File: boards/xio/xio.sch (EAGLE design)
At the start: 295 parts, among them CN3 J00-0065NL, U2 LAN8742A-CZ, X2 USB-A, Y1 NX3225SA-12.000MHZ-STD-CSR-1, Y2 NX3225SA-12.000MHZ-STD-CSR-1, Y3 NX3225SA-25.000MHZ-STD-CSR-1

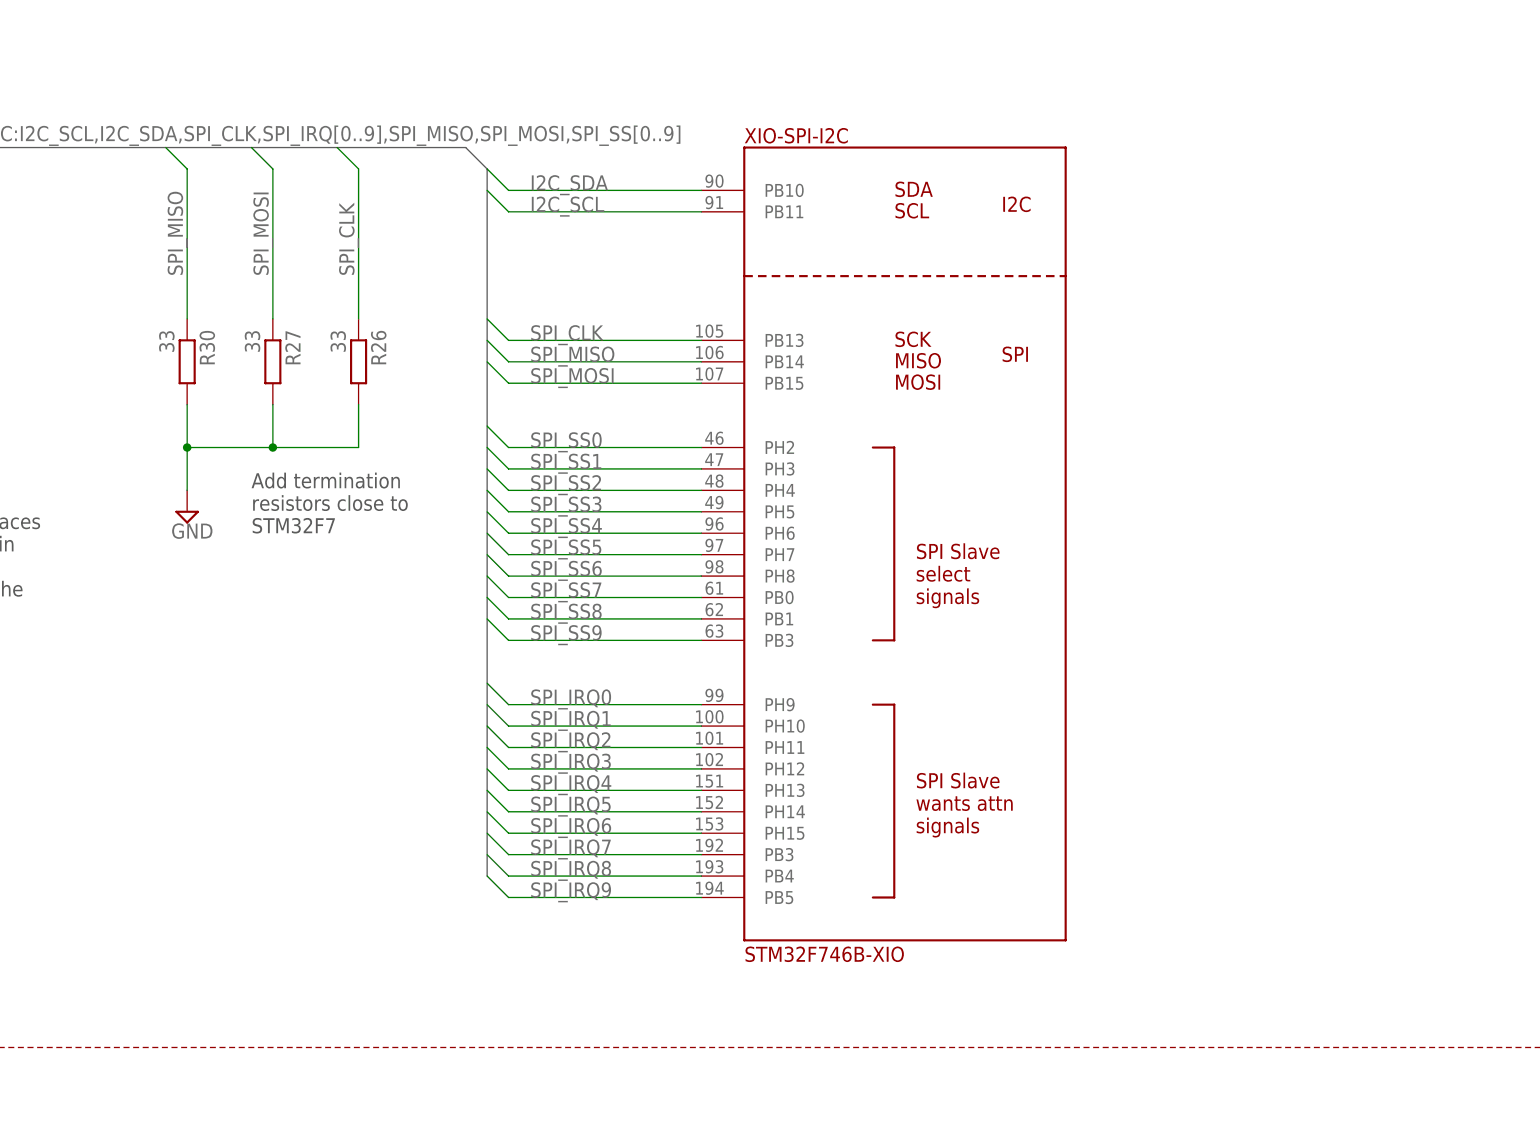
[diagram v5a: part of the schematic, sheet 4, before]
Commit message: Update schematics regarding comments and unroute board
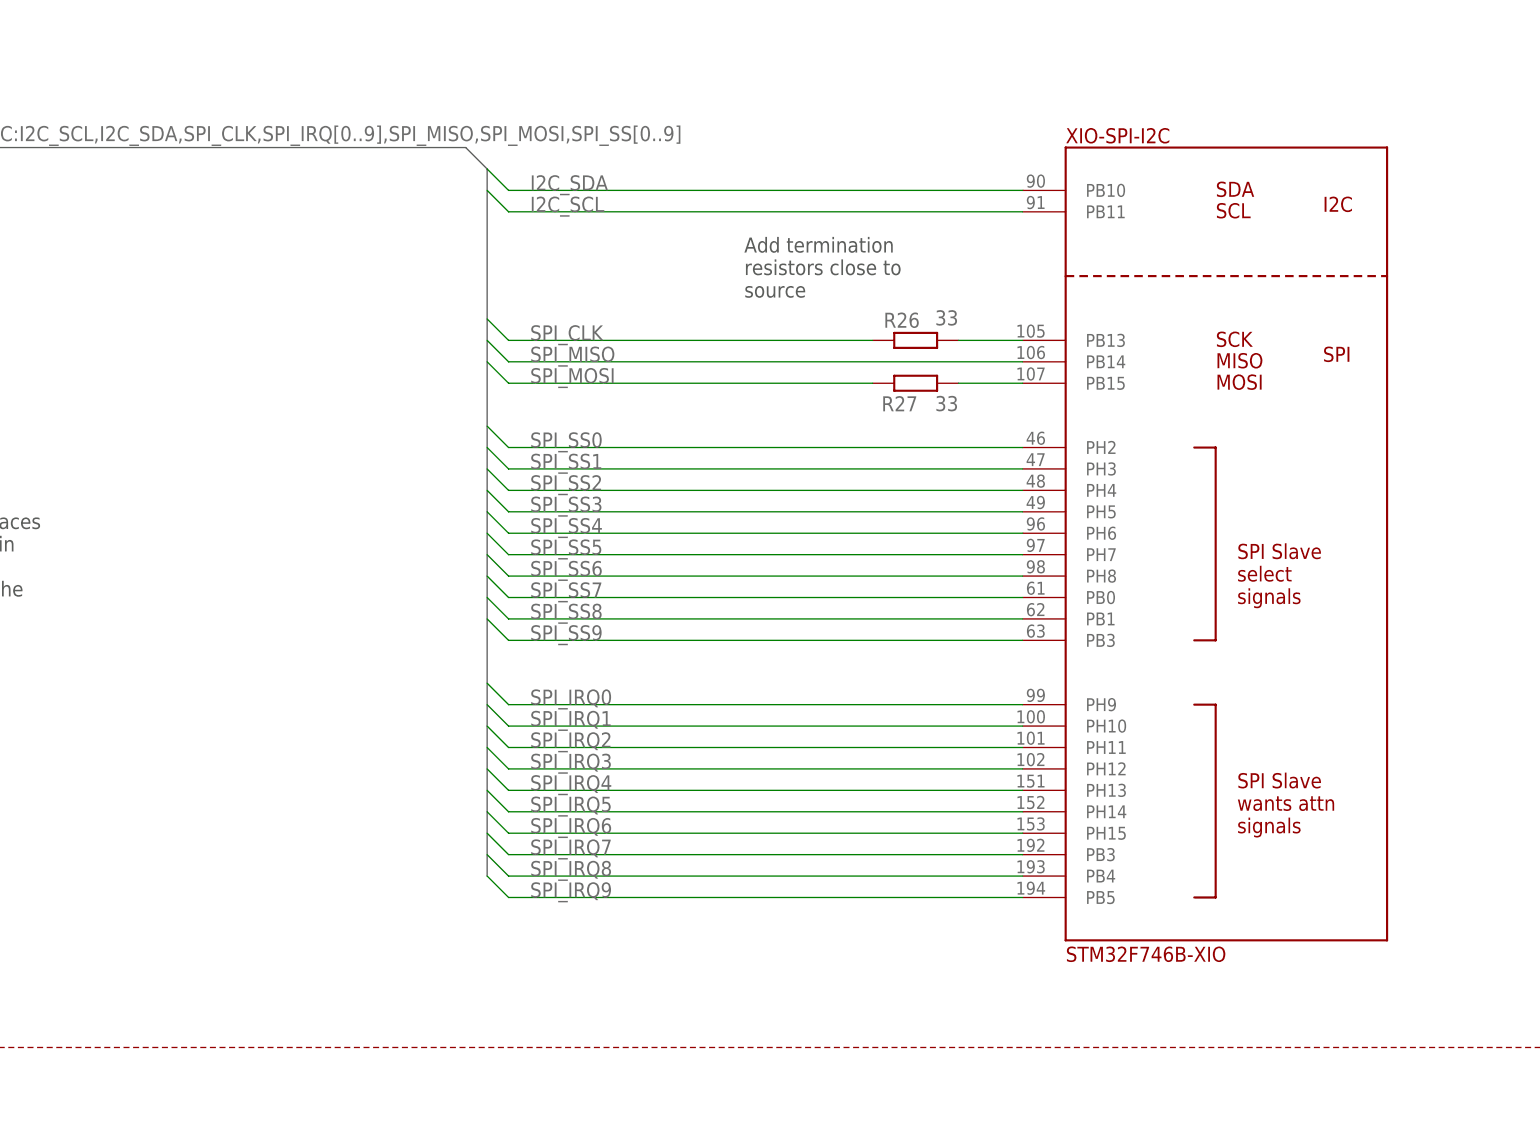
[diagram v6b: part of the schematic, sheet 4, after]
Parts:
- removed R30: 33, rcl:R-EU_R0402
- added R91: 33, rcl:R-EU_R0402
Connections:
- new net N$57: R26.2, XIO-SPI-I2C.PB13@105
- new net N$61: R27.2, XIO-SPI-I2C.PB15@107
- new net PIO_VDDA: C57.1, C58.1, PIO-POWER.VDDA@42, PIO-POWER.VREF+@41, R91.2
- net +3V3: now also R91.1; no longer C1.1, C13.1, C57.1, C58.1, PIO-POWER.VDDA@42, PIO-POWER.VREF+@41, XIO-POWER.VREF+@41
- net GND: no longer R26.2, R27.2, R30.2
- net SPI_CLK: no longer XIO-SPI-I2C.PB13@105
- net SPI_MISO: no longer R30.1
- net SPI_MOSI: no longer XIO-SPI-I2C.PB15@107
- net XIO_VDDA: now also C1.1, C13.1, XIO-POWER.VREF+@41
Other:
- note added: "- Added capacitor to +3v3 on SD_SLOT"
- note added: "- Added resistor in series to power on VDDA - Added pull-ups on /RESET and SWDIO - Added 0-ohm resistors on all power sources"
- note added: "Add termination resistors close to source"
- note added: "Filter on VDDA"
- note added: "Need ESD"
- note removed: "- Added capacitor to +3v3 on SD_SLOT - is 0.1uF sufficient ?"
- note removed: "- Added resistor in series to power on VDDA - is 33R ok ? - Added pull-ups on /RESET and SWDIO - Added 0-ohm resistors on all power sources"
- note removed: "- Need ESD ? What to do ?"
- note removed: "Add termination resistors close to STM32F7"
- note removed: "Anoop says "mended to add a filter on micro’s VDDA pin and connect the filter cap between VDDA and VSSA" - need to understand more"
- moved on the sheet: C1, C13, C57, C58, R21, R26, R27, XIO-SPI-I2C

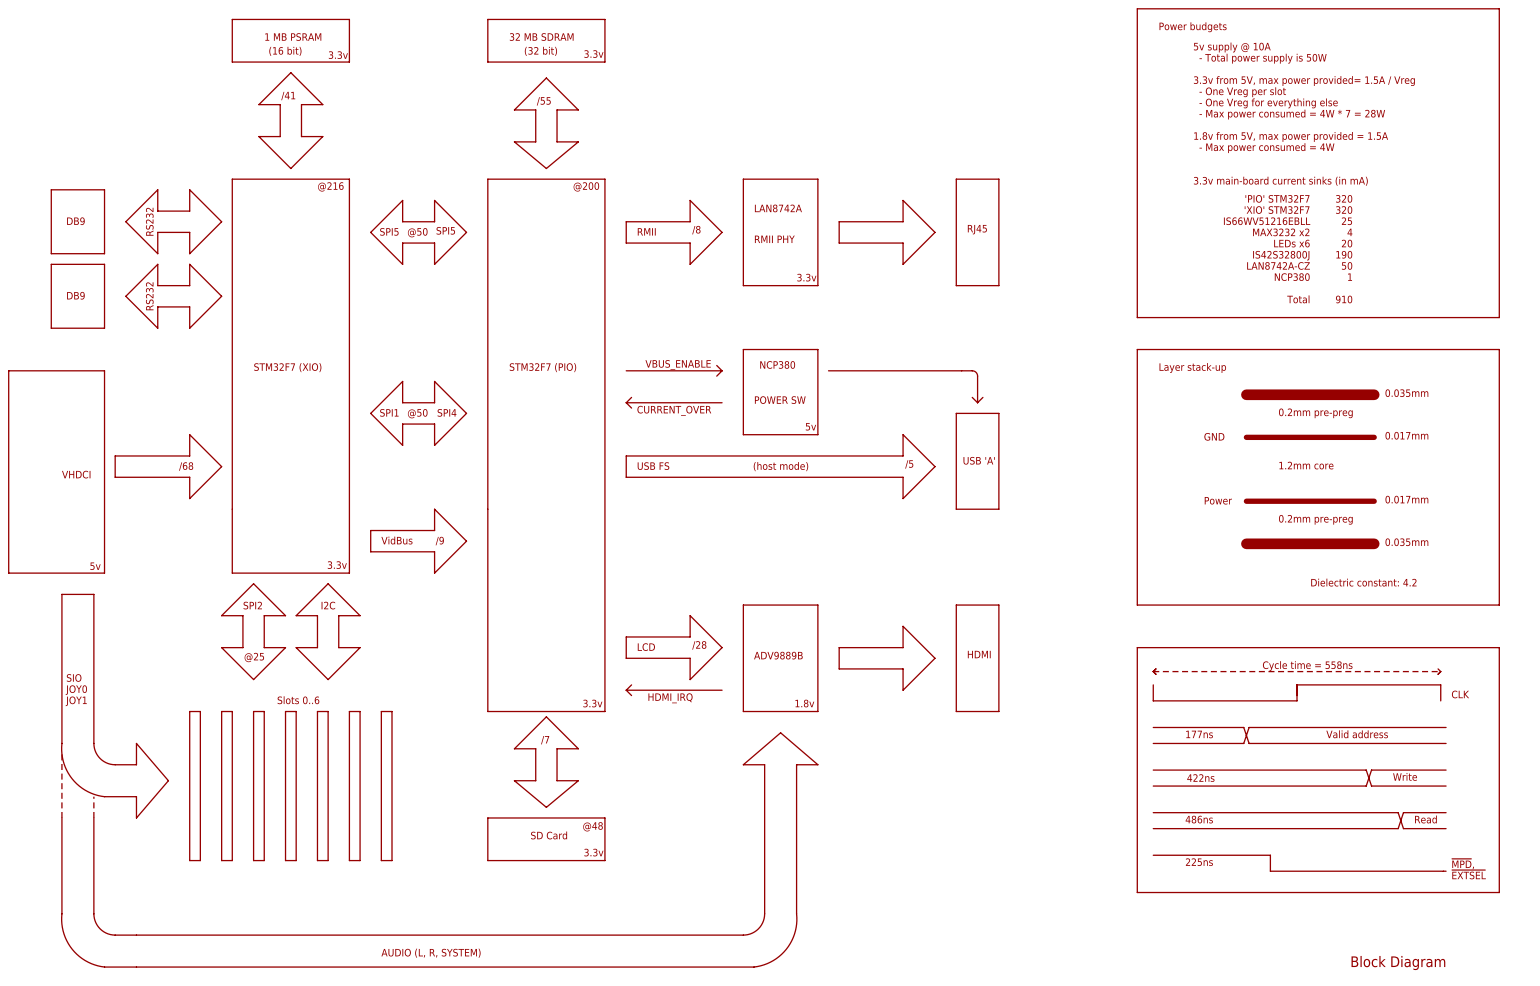
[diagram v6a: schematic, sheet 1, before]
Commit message: Start to patch in the H processor for XIO
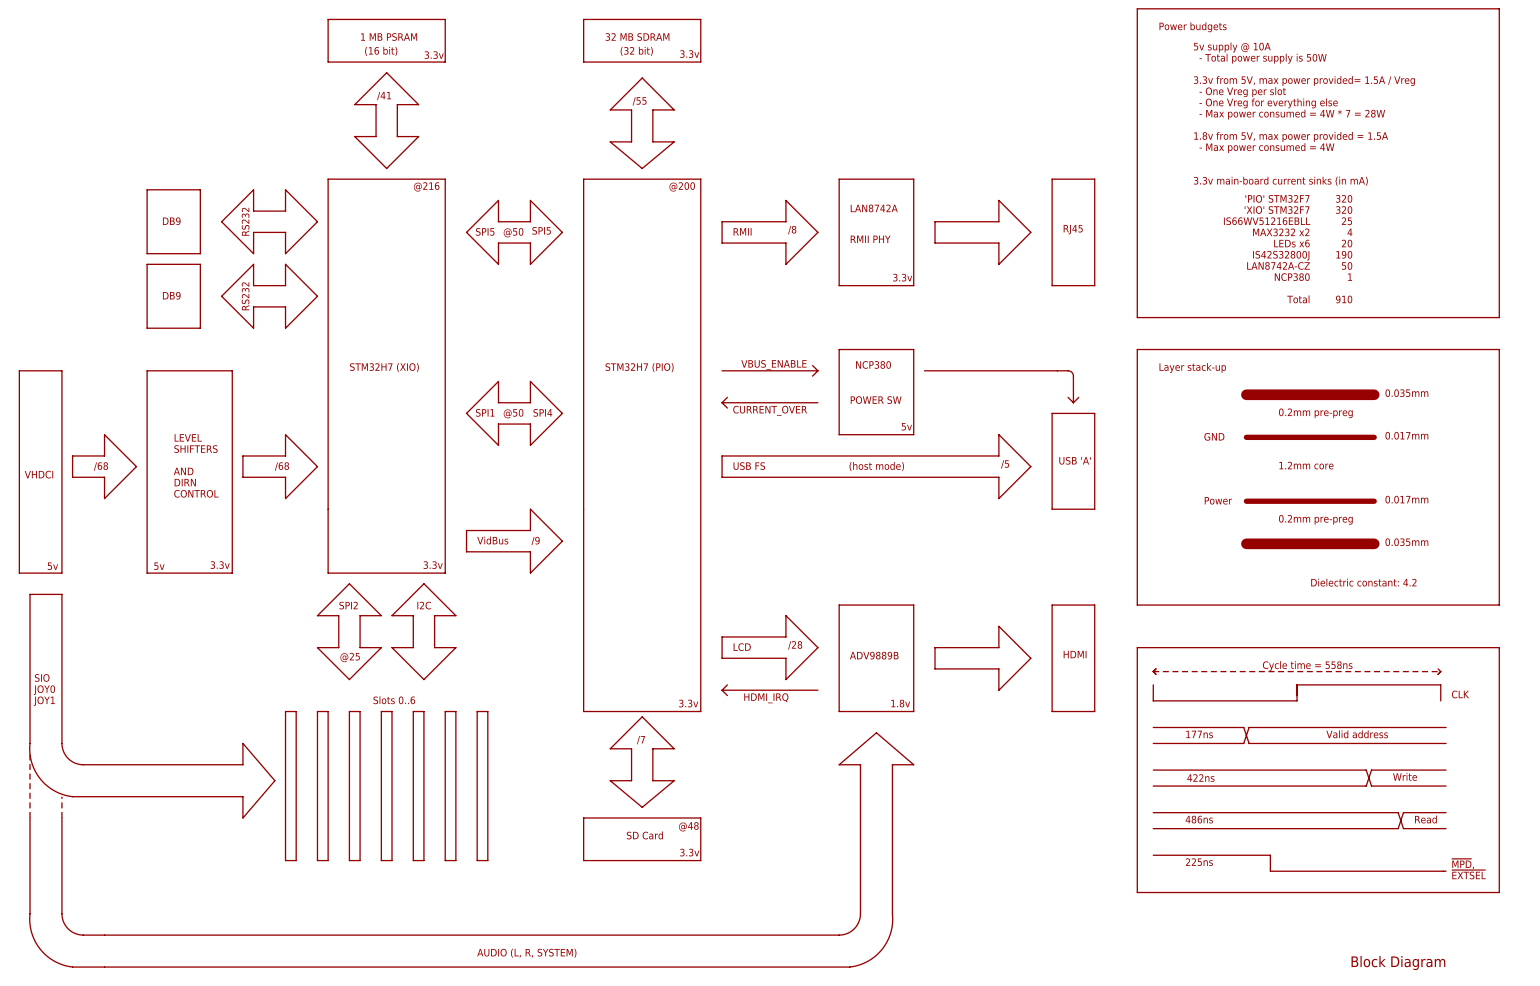
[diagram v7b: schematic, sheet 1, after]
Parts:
- removed R52: 33, rcl:R-EU_R0402
- XIO: value STM32F746B-XIO -> STM32H753B-XIO; device sjg-stm32:STM32F746B-XIO -> sjg-stm32:STM32H753B-XIO
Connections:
- removed net N$21: R52.2, XIO-VBUS.PJ15@177
- net !RESET!: now also XIO-PWR.!RST!@34; no longer XIO-POWER.!RST!@34
- net !VHDCI_EXSEL!: no longer XIO-VHDCI.PI8@7
- net !VHDCI_IRQ!: no longer XIO-VHDCI.PI9@11
- net !VHDCI_MPD!: no longer XIO-VHDCI.PI10@12
- net +3V3: now also XIO-PWR.VBAT@6, XIO-PWR.VDD@103, XIO-PWR.VDD@115, XIO-PWR.VDD@124, XIO-PWR.VDD@15, XIO-PWR.VDD@150, XIO-PWR.VDD@158, XIO-PWR.VDD@171, XIO-PWR.VDD@185, XIO-PWR.VDD@204, XIO-PWR.VDD@26, XIO-PWR.VDD@39, XIO-PWR.VDD@52, XIO-PWR.VDD@59, XIO-PWR.VDD@73, XIO-PWR.VDD@83, XIO-PWR.VDD@94, XIO-PWR.VDDUSB@137; no longer XIO-POWER.VBAT@6, XIO-POWER.VDD@103, XIO-POWER.VDD@115, XIO-POWER.VDD@124, XIO-POWER.VDD@15, XIO-POWER.VDD@150, XIO-POWER.VDD@158, XIO-POWER.VDD@171, XIO-POWER.VDD@185, XIO-POWER.VDD@204, XIO-POWER.VDD@26, XIO-POWER.VDD@39, XIO-POWER.VDD@52, XIO-POWER.VDD@59, XIO-POWER.VDD@73, XIO-POWER.VDD@83, XIO-POWER.VDD@94, XIO-POWER.VDDUSB@137
- net ARCH0: no longer XIO-CFG.PE2@1
- net ARCH1: no longer XIO-CFG.PE3@2
- net ARCH2: no longer XIO-CFG.PE4@3
- net ARCH3: no longer XIO-CFG.PE5@4
- net GND: now also XIO-PWR.VSS@114, XIO-PWR.VSS@125, XIO-PWR.VSS@136, XIO-PWR.VSS@14, XIO-PWR.VSS@149, XIO-PWR.VSS@170, XIO-PWR.VSS@184, XIO-PWR.VSS@202, XIO-PWR.VSS@25, XIO-PWR.VSS@51, XIO-PWR.VSS@60, XIO-PWR.VSS@72, XIO-PWR.VSS@82, XIO-PWR.VSS@93, XIO-PWR.VSSA@40; no longer XIO-POWER.VSS@114, XIO-POWER.VSS@125, XIO-POWER.VSS@136, XIO-POWER.VSS@14, XIO-POWER.VSS@149, XIO-POWER.VSS@170, XIO-POWER.VSS@184, XIO-POWER.VSS@202, XIO-POWER.VSS@25, XIO-POWER.VSS@51, XIO-POWER.VSS@60, XIO-POWER.VSS@72, XIO-POWER.VSS@82, XIO-POWER.VSS@93, XIO-POWER.VSSA@40
- net I2C_SCL: now also XIO-SPI_I2C.PB11@91; no longer XIO-SPI-I2C.PB11@91
- net I2C_SDA: now also XIO-SPI_I2C.PB10@90; no longer XIO-SPI-I2C.PB10@90
- net MEM0: no longer XIO-CFG.PF10@31
- net MEM1: no longer XIO-CFG.PF11@70
- net N$1: now also XIO-PWR.PH1@33; no longer XIO-POWER.PH1@33
- net N$11: now also XIO-PWR.BOOT0@197; no longer XIO-POWER.BOOT0@197
- net N$13: now also XIO-LED.PD5@169; no longer XIO-LED.PD2@166
- net N$14: now also XIO-LED.PD6@172; no longer XIO-LED.PD3@167
- net N$15: now also XIO-LED.PD7@173; no longer XIO-LED.PD6@172
- net N$18: no longer XIO-VHDCI.PJ0@65
- net N$2: now also XIO-PWR.PH0@32; no longer XIO-POWER.PH0@32
- net N$3: now also XIO-PWR.VCAP1@92; no longer XIO-POWER.VCAP1@92
- net N$34: now also XIO-USART.PA0@43; no longer XIO-UART.PA0@43
- net N$35: now also XIO-USART.PA3@50; no longer XIO-UART.PA3@50
- net N$39: now also XIO-USART.PA2@45; no longer XIO-UART.PA2@45
- net N$40: now also XIO-USART.PA1@44; no longer XIO-UART.PA1@44
- net N$47: now also XIO-USART.PG13@182; no longer XIO-UART.PG13@182
- net N$48: now also XIO-USART.PG9@178; no longer XIO-UART.PG9@178
- net N$49: now also XIO-USART.PG14@183; no longer XIO-UART.PG14@183
- net N$5: now also XIO-PWR.VCAP2@148; no longer XIO-POWER.VCAP2@148
- net N$50: now also XIO-USART.PG12@181; no longer XIO-UART.PG12@181
- net N$57: now also XIO-SPI_I2C.PB13@105; no longer XIO-SPI-I2C.PB13@105
- net N$61: now also XIO-SPI_I2C.PB15@107; no longer XIO-SPI-I2C.PB15@107
- net N$7: now also XIO-PWR.PDR_ON@203; no longer XIO-POWER.PDR_ON@203
- net PID0: no longer XIO-CFG.PG10@179
- net PID1: no longer XIO-CFG.PG11@180
- net PID2: no longer XIO-CFG.PG15@191
- net SPI_IRQ0: now also XIO-SPI_I2C.PH9@99; no longer XIO-SPI-I2C.PH9@99
- net SPI_IRQ1: now also XIO-SPI_I2C.PH10@100; no longer XIO-SPI-I2C.PH10@100
- net SPI_IRQ2: now also XIO-SPI_I2C.PH11@101; no longer XIO-SPI-I2C.PH11@101
- net SPI_IRQ3: now also XIO-SPI_I2C.PH12@102; no longer XIO-SPI-I2C.PH12@102
- net SPI_IRQ4: now also XIO-SPI_I2C.PH13@151; no longer XIO-SPI-I2C.PH13@151
- net SPI_IRQ5: now also XIO-SPI_I2C.PH14@152; no longer XIO-SPI-I2C.PH14@152
- net SPI_IRQ6: now also XIO-SPI_I2C.PH15@153; no longer XIO-SPI-I2C.PH15@153
- net SPI_IRQ7: now also XIO-SPI_I2C.PB5@194; no longer XIO-SPI-I2C.PB3@192
- net SPI_IRQ8: now also XIO-SPI_I2C.PG6@133; no longer XIO-SPI-I2C.PB4@193
- net SPI_IRQ9: now also XIO-SPI_I2C.PG7@134; no longer XIO-SPI-I2C.PB5@193
- net SPI_MISO: now also XIO-SPI_I2C.PB14@106; no longer XIO-SPI-I2C.PB14@106
- net SPI_SS0: now also XIO-SPI_I2C.PH2@46; no longer XIO-SPI-I2C.PH2@46
- net SPI_SS1: now also XIO-SPI_I2C.PH3@47; no longer XIO-SPI-I2C.PH3@47
- net SPI_SS2: now also XIO-SPI_I2C.PH4@48; no longer XIO-SPI-I2C.PH4@48
- net SPI_SS3: now also XIO-SPI_I2C.PG3@130; no longer XIO-SPI-I2C.PH5@49
- net SPI_SS4: now also XIO-SPI_I2C.PH6@96; no longer XIO-SPI-I2C.PH6@96
- net SPI_SS5: now also XIO-SPI_I2C.PH7@97; no longer XIO-SPI-I2C.PH7@97
- net SPI_SS6: now also XIO-SPI_I2C.PH8@98; no longer XIO-SPI-I2C.PH8@98
- net SPI_SS7: now also XIO-SPI_I2C.PD11@111; no longer XIO-SPI-I2C.PB0@61
- net SPI_SS8: now also XIO-SPI_I2C.PD12@112; no longer XIO-SPI-I2C.PB1@62
- net SPI_SS9: now also XIO-SPI_I2C.PD13@113; no longer XIO-SPI-I2C.PB3@63
- net VHDCI_A0: no longer XIO-VHDCI.PC0@35
- net VHDCI_A1: no longer XIO-VHDCI.PC1@36
- net VHDCI_A10: no longer XIO-VHDCI.PC10@161
- net VHDCI_A11: no longer XIO-VHDCI.PC11@162
- net VHDCI_A12: no longer XIO-VHDCI.PC12@163
- net VHDCI_A13: no longer XIO-VHDCI.PC13@8
- net VHDCI_A14: no longer XIO-VHDCI.PC14@9
- net VHDCI_A15: no longer XIO-VHDCI.PC15@10
- net VHDCI_A2: no longer XIO-VHDCI.PC2@37
- net VHDCI_A3: no longer XIO-VHDCI.PC3@38
- net VHDCI_A4: no longer XIO-VHDCI.PC4@57
- net VHDCI_A5: no longer XIO-VHDCI.PC5@58
- net VHDCI_A6: no longer XIO-VHDCI.PC6@138
- net VHDCI_A7: no longer XIO-VHDCI.PC7@139
- net VHDCI_A8: no longer XIO-VHDCI.PC8@140
- net VHDCI_A9: no longer XIO-VHDCI.PC9@141
- net VHDCI_CCTL: no longer XIO-VHDCI.PI11@13
- net VHDCI_CLK: no longer XIO-VHDCI.PI12@19
- net VHDCI_D0: no longer XIO-VHDCI.PI0@154
- net VHDCI_D1: no longer XIO-VHDCI.PI1@155
- net VHDCI_D1XX: no longer XIO-VHDCI.PI13@20
- net VHDCI_D2: no longer XIO-VHDCI.PI2@156
- net VHDCI_D3: no longer XIO-VHDCI.PI3@157
- net VHDCI_D4: no longer XIO-VHDCI.PI4@205
- net VHDCI_D5: no longer XIO-VHDCI.PI5@206
- net VHDCI_D6: no longer XIO-VHDCI.PI6@207
- net VHDCI_D7: no longer XIO-VHDCI.PI7@208
- net VHDCI_HALT: no longer XIO-VHDCI.PI14@21
- net VHDCI_RD4: no longer XIO-VHDCI.PI15@64
- net VHDCI_RD5: no longer XIO-VHDCI.PJ1@66
- net VHDCI_REF: no longer XIO-VHDCI.PJ2@67
- net VHDCI_RSRVD0: no longer XIO-VHDCI.PJ3@68
- net VHDCI_RSRVD1: no longer XIO-VHDCI.PJ4@69
- net VHDCI_RSRVD2: no longer XIO-VHDCI.PJ5@95
- net VHDCI_RSRVD3: no longer XIO-VHDCI.PJ6@118
- net VHDCI_RSRVD4: no longer XIO-VHDCI.PJ7@119
- net VHDCI_RSRVD5: no longer XIO-VHDCI.PJ8@120
- net VHDCI_RSRVD6: no longer XIO-VHDCI.PJ9@121
- net VHDCI_RST: no longer XIO-VHDCI.PJ10@122
- net VHDCI_RW: no longer XIO-VHDCI.PJ11@123
- net VHDCI_S4: no longer XIO-VHDCI.PJ12@174
- net VHDCI_S5: no longer XIO-VHDCI.PJ13@175
- net VIDBUS_0: no longer XIO-VBUS.PK0@126
- net VIDBUS_1: no longer XIO-VBUS.PK1@127
- net VIDBUS_2: no longer XIO-VBUS.PK2@128
- net VIDBUS_3: no longer XIO-VBUS.PK3@186
- net VIDBUS_4: no longer XIO-VBUS.PK4@187
- net VIDBUS_5: no longer XIO-VBUS.PK5@188
- net VIDBUS_6: no longer XIO-VBUS.PK6@189
- net VIDBUS_7: no longer XIO-VBUS.PK7@190
- net VIDBUS_CLK: no longer R52.1
- net XIO_RAM_!CS!: no longer XIO-PSRAM.PD7@173
- net XIO_RAM_!LB!: no longer XIO-PSRAM.PE0@200
- net XIO_RAM_!OE!: no longer XIO-PSRAM.PD4@168
- net XIO_RAM_!UB!: no longer XIO-PSRAM.PE1@201
- net XIO_RAM_!WE!: no longer XIO-PSRAM.PD5@169
- net XIO_RAM_A0: no longer XIO-PSRAM.PF0@16
- net XIO_RAM_A1: no longer XIO-PSRAM.PF1@17
- net XIO_RAM_A10: no longer XIO-PSRAM.PG0@77
- net XIO_RAM_A11: no longer XIO-PSRAM.PG1@78
- net XIO_RAM_A12: no longer XIO-PSRAM.PG2@129
- net XIO_RAM_A13: no longer XIO-PSRAM.PG3@130
- net XIO_RAM_A14: no longer XIO-PSRAM.PG4@131
- net XIO_RAM_A15: no longer XIO-PSRAM.PG5@132
- net XIO_RAM_A16: no longer XIO-PSRAM.PD11@111
- net XIO_RAM_A17: no longer XIO-PSRAM.PD12@112
- net XIO_RAM_A18: no longer XIO-PSRAM.PD13@113
- net XIO_RAM_A2: no longer XIO-PSRAM.PF2@18
- net XIO_RAM_A3: no longer XIO-PSRAM.PF3@22
- net XIO_RAM_A4: no longer XIO-PSRAM.PF4@23
- net XIO_RAM_A5: no longer XIO-PSRAM.PF5@24
- net XIO_RAM_A6: no longer XIO-PSRAM.PF12@71
- net XIO_RAM_A7: no longer XIO-PSRAM.PF13@74
- net XIO_RAM_A8: no longer XIO-PSRAM.PF14@75
- net XIO_RAM_A9: no longer XIO-PSRAM.PF15@76
- net XIO_RAM_D0: no longer XIO-PSRAM.PD14@116
- net XIO_RAM_D1: no longer XIO-PSRAM.PD15@117
- net XIO_RAM_D10: no longer XIO-PSRAM.PE13@87
- net XIO_RAM_D11: no longer XIO-PSRAM.PE14@88
- net XIO_RAM_D12: no longer XIO-PSRAM.PE15@89
- net XIO_RAM_D13: no longer XIO-PSRAM.PD8@108
- net XIO_RAM_D14: no longer XIO-PSRAM.PD9@109
- net XIO_RAM_D15: no longer XIO-PSRAM.PD10@110
- net XIO_RAM_D2: no longer XIO-PSRAM.PD0@164
- net XIO_RAM_D3: no longer XIO-PSRAM.PD1@165
- net XIO_RAM_D4: no longer XIO-PSRAM.PE7@79
- net XIO_RAM_D5: no longer XIO-PSRAM.PE8@80
- net XIO_RAM_D6: no longer XIO-PSRAM.PE9@81
- net XIO_RAM_D7: no longer XIO-PSRAM.PE10@84
- net XIO_RAM_D8: no longer XIO-PSRAM.PE11@85
- net XIO_RAM_D9: no longer XIO-PSRAM.PE12@86
- net XIO_RX: now also XIO-PWR.PB7@196; no longer XIO-POWER.PB7@196
- net XIO_SWDCLK: now also XIO-PWR.PA14@159; no longer XIO-POWER.PA14@159
- net XIO_SWDIO: now also XIO-PWR.PA13@147; no longer XIO-POWER.PA13@147
- net XIO_TX: now also XIO-PWR.PB6@195; no longer XIO-POWER.PB6@195
- net XIO_VDDA: now also XIO-PWR.VDDA@42, XIO-PWR.VREF+@41; no longer XIO-POWER.VDDA@42, XIO-POWER.VREF+@41
- net XSPI1_CLK: no longer XIO-XSPI.PA5@54
- net XSPI1_MISO: no longer XIO-XSPI.PA6@55
- net XSPI1_MOSI: no longer XIO-XSPI.PA7@56
- net XSPI1_SSEL: no longer XIO-XSPI.PA4@53
- net XSPI2_CLK: no longer XIO-XSPI.PF7@28
- net XSPI2_MISO: no longer XIO-XSPI.PF8@29
- net XSPI2_MOSI: no longer XIO-XSPI.PF9@30
- net XSPI2_SSEL: no longer XIO-XSPI.PF6@27
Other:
- note added: "LEVEL SHIFTERS AND DIRN CONTROL"
- note added: "STM32H7 (PIO)"
- note added: "STM32H7 (XIO)"
- note removed: "STM32F7 (PIO)"
- note removed: "STM32F7 (XIO)"
- note removed: "Series termination resistor Placed close to source"
- note removed: "Video bus out"
